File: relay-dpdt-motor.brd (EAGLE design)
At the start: 81.3 x 28.9 mm, 11 parts, among them J1 1X2-3.5MM, J2 1X2-3.5MM, K1 4052, K2 4052

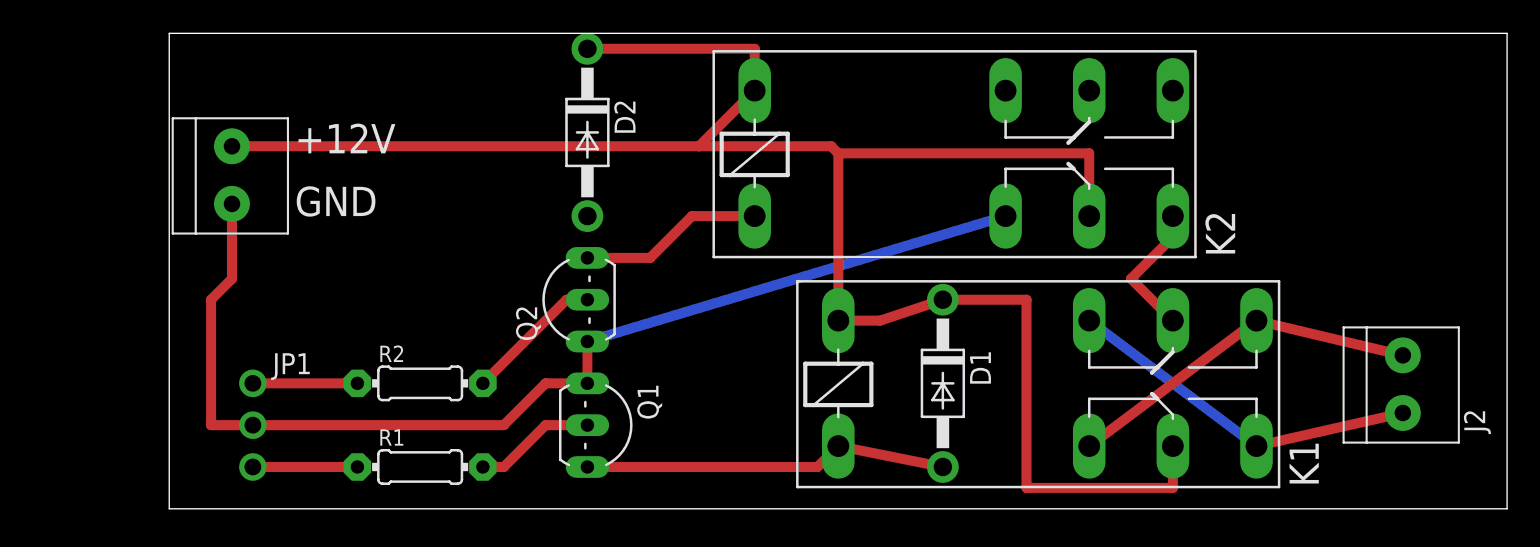
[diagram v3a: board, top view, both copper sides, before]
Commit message: 2 relays one cup, new sim
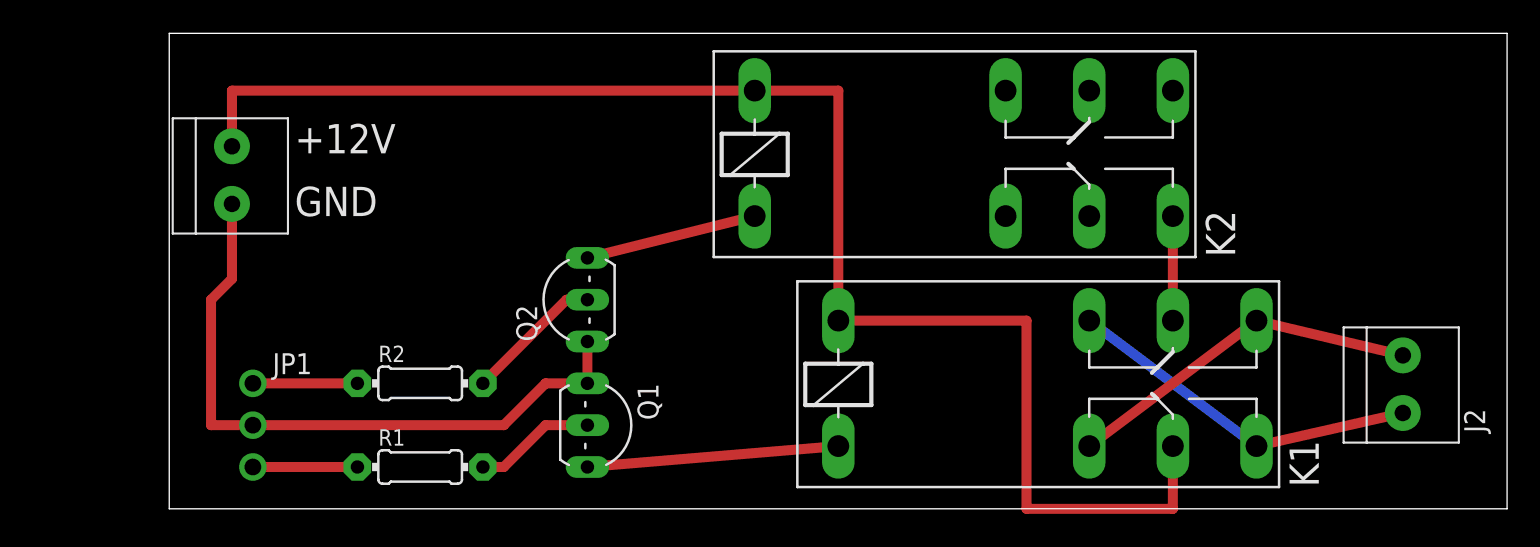
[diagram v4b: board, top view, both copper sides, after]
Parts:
- removed D1, D2: 1N4004, adafruit:DO41-10
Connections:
- removed net N$2: D1.A, K1.2, Q1.3
- new net N$4: K2.2, Q2.3
- net +12V: no longer D1.C, D2.C, K2.P1
- net GND: now also K2.P1; no longer K2.O1
- net N$8: now also K1.2, Q1.3; no longer D2.A, K2.2, Q2.3
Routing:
- net +12V: track 118.2 -> 89.7 mm
- net GND: track 66.9 -> 40.4 mm
- net N$2: track 22.2 -> 0.00 mm
- net N$4: track 0.00 -> 10.5 mm
- net N$8: track 11.2 -> 15.3 mm
- net N$10: track 8.45 -> 6.35 mm
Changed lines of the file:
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@@
 <element name="Q1" library="dp_devices" package="TO-92" value="" x="25.4" y="5.08" rot="R270"/>
 <element name="R1" library="adafruit" package="0204/7" value="" x="15.24" y="2.54"/>
-<element name="D1" library="adafruit" package="DO41-10" value="1N4004" x="46.99" y="7.62" rot="R270"/>
 <element name="J1" library="adafruit" package="1X2-3.5MM" value="1X2-3.5MM" x="3.81" y="20.32" smashed="yes" rot="R270"/>
 <element name="R2" library="adafruit" package="0204/7" value="" x="15.24" y="7.62"/>
@@
 </element>
 <element name="Q2" library="dp_devices" package="TO-92" value="" x="25.4" y="12.7" rot="R90"/>
-<element name="D2" library="adafruit" package="DO41-10" value="1N4004" x="25.4" y="22.86" rot="R270"/>
 </elements>
 <signals>
@@
 <contactref element="K1" pad="P1"/>
 <contactref element="K1" pad="1"/>
-<wire x1="3.81" y1="22.02" x2="32.18" y2="22.02" width="0.6096" layer="1"/>
-<wire x1="32.18" y1="22.02" x2="35.56" y2="25.4" width="0.6096" layer="1"/>
-<wire x1="32.18" y1="22.02" x2="40.21" y2="22.02" width="0.6096" layer="1"/>
-<wire x1="40.21" y1="22.02" x2="40.64" y2="21.59" width="0.6096" layer="1"/>
-<wire x1="40.64" y1="21.59" x2="40.64" y2="11.43" width="0.6096" layer="1"/>
-<wire x1="40.64" y1="11.43" x2="43.18" y2="11.43" width="0.6096" layer="1"/>
-<contactref element="D1" pad="C"/>
-<contactref element="D2" pad="C"/>
-<wire x1="25.4" y1="27.94" x2="35.56" y2="27.94" width="0.6096" layer="1"/>
-<wire x1="35.56" y1="27.94" x2="35.56" y2="25.4" width="0.6096" layer="1"/>
-<wire x1="43.18" y1="11.43" x2="46.99" y2="12.7" width="0.6096" layer="1"/>
-<contactref element="K2" pad="P1"/>
-<wire x1="55.88" y1="17.78" x2="55.88" y2="21.59" width="0.6096" layer="1"/>
-<wire x1="55.88" y1="21.59" x2="40.64" y2="21.59" width="0.6096" layer="1"/>
-<wire x1="60.96" y1="3.81" x2="60.96" y2="1.27" width="0.6096" layer="1"/>
-<wire x1="60.96" y1="1.27" x2="52.07" y2="1.27" width="0.6096" layer="1"/>
-<wire x1="52.07" y1="1.27" x2="52.07" y2="12.7" width="0.6096" layer="1"/>
-<wire x1="52.07" y1="12.7" x2="46.99" y2="12.7" width="0.6096" layer="1"/>
-</signal>
-<signal name="N$2">
-<contactref element="K1" pad="2"/>
-<contactref element="Q1" pad="3"/>
-<wire x1="25.4" y1="2.54" x2="39.37" y2="2.54" width="0.6096" layer="1"/>
-<wire x1="39.37" y1="2.54" x2="40.64" y2="3.81" width="0.6096" layer="1"/>
-<contactref element="D1" pad="A"/>
-<wire x1="40.64" y1="3.81" x2="46.99" y2="2.54" width="0.6096" layer="1"/>
+<wire x1="3.81" y1="22.02" x2="3.81" y2="25.4" width="0.6096" layer="1"/>
+<wire x1="3.81" y1="25.4" x2="35.56" y2="25.4" width="0.6096" layer="1"/>
+<wire x1="35.56" y1="25.4" x2="40.64" y2="25.4" width="0.6096" layer="1"/>
+<wire x1="40.64" y1="25.4" x2="40.64" y2="11.43" width="0.6096" layer="1"/>
+<wire x1="40.64" y1="11.43" x2="52.07" y2="11.43" width="0.6096" layer="1"/>
+<wire x1="60.96" y1="3.81" x2="60.96" y2="0" width="0.6096" layer="1"/>
+<wire x1="60.96" y1="0" x2="52.07" y2="0" width="0.6096" layer="1"/>
+<wire x1="52.07" y1="0" x2="52.07" y2="11.43" width="0.6096" layer="1"/>
 </signal>
 <signal name="GND">
@@
 <contactref element="J1" pad="1"/>
 <contactref element="Q2" pad="1"/>
-<contactref element="K2" pad="O1"/>
 <contactref element="JP1" pad="2"/>
 <wire x1="3.81" y1="18.52" x2="3.81" y2="13.97" width="0.6096" layer="1"/>
@@
 <wire x1="22.86" y1="7.62" x2="25.4" y2="7.62" width="0.6096" layer="1"/>
 <wire x1="25.4" y1="10.16" x2="25.4" y2="7.62" width="0.6096" layer="1"/>
-<wire x1="25.4" y1="10.16" x2="50.8" y2="17.78" width="0.6096" layer="16"/>
+<contactref element="K2" pad="P1"/>
+<wire x1="25.4" y1="10.16" x2="55.88" y2="17.78" width="0" layer="19" extent="1-1"/>
 </signal>
 <signal name="N$3">
@@
 <wire x1="5.08" y1="7.62" x2="11.43" y2="7.62" width="0.6096" layer="1"/>
 </signal>
-<signal name="N$8">
-<contactref element="K2" pad="2"/>
-<contactref element="Q2" pad="3"/>
-<wire x1="25.4" y1="15.24" x2="29.21" y2="15.24" width="0.6096" layer="1"/>
-<wire x1="29.21" y1="15.24" x2="31.75" y2="17.78" width="0.6096" layer="1"/>
-<wire x1="31.75" y1="17.78" x2="35.56" y2="17.78" width="0.6096" layer="1"/>
-<contactref element="D2" pad="A"/>
-<wire x1="25.4" y1="15.24" x2="25.4" y2="17.78" width="0" layer="19" extent="1-1"/>
-</signal>
 <signal name="N$10">
 <contactref element="K1" pad="P2"/>
 <contactref element="K2" pad="S1"/>
-<wire x1="58.42" y1="13.97" x2="60.96" y2="11.43" width="0.6096" layer="1"/>
-<wire x1="60.96" y1="17.78" x2="60.96" y2="16.51" width="0.6096" layer="1"/>
-<wire x1="60.96" y1="16.51" x2="58.42" y2="13.97" width="0.6096" layer="1"/>
+<wire x1="60.96" y1="17.78" x2="60.96" y2="11.43" width="0.6096" layer="1"/>
+</signal>
+<signal name="N$4">
+<contactref element="Q2" pad="3"/>
+<contactref element="K2" pad="2"/>
+<wire x1="25.4" y1="15.24" x2="35.56" y2="17.78" width="0.6096" layer="1"/>
+</signal>
+<signal name="N$8">
+<contactref element="Q1" pad="3"/>
+<contactref element="K1" pad="2"/>
+<wire x1="25.4" y1="2.54" x2="40.64" y2="3.81" width="0.6096" layer="1"/>
 </signal>
 </signals>

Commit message: working relay, but i returned to using the monstermotor shield. and now with beter stop code for the motors
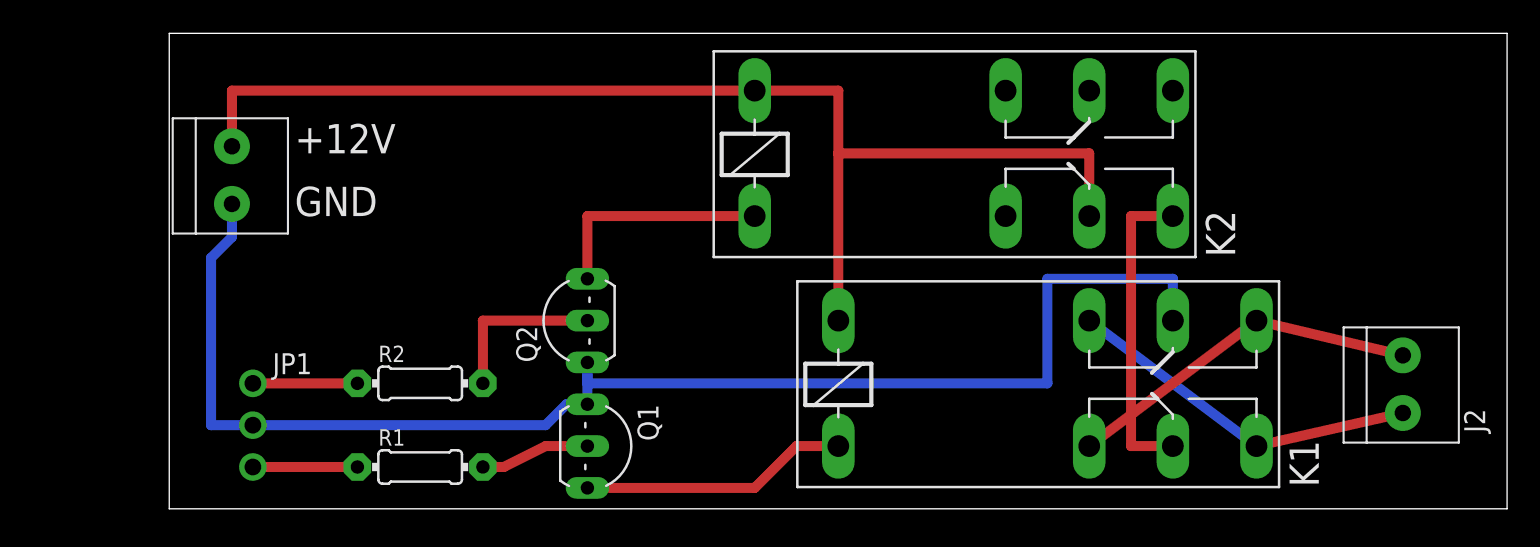
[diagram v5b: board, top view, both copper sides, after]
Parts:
- moved Q1 1.27 mm to (25.4, 3.81)
- moved Q2 1.27 mm to (25.4, 11.4)
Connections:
- removed net N$10: K1.P2, K2.S1
- new net N$2: K1.P1, K2.S1
- net +12V: now also K2.P1; no longer K1.P1
- net GND: now also K1.P2; no longer K2.P1
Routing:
- net GND: track 40.4 -> 85.6 mm
- net N$2: track 0.00 -> 19.0 mm
- net +12V: track 89.7 -> 73.2 mm
- net N$10: track 6.35 -> 0.00 mm
- net N$4: track 10.5 -> 14.0 mm
- net N$3: track 8.45 -> 10.2 mm
- net N$8: track 15.3 -> 16.3 mm
- net N$1: track 7.40 -> 6.65 mm
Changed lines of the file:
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@@
 <attribute name="OC_FARNELL" value="unknown" x="44.45" y="7.62" size="1.778" layer="27" display="off"/>
 </element>
-<element name="Q1" library="dp_devices" package="TO-92" value="" x="25.4" y="5.08" rot="R270"/>
+<element name="Q1" library="dp_devices" package="TO-92" value="" x="25.4" y="3.81" rot="R270"/>
 <element name="R1" library="adafruit" package="0204/7" value="" x="15.24" y="2.54"/>
 <element name="J1" library="adafruit" package="1X2-3.5MM" value="1X2-3.5MM" x="3.81" y="20.32" smashed="yes" rot="R270"/>
@@
 <attribute name="OC_FARNELL" value="unknown" x="39.37" y="21.59" size="1.778" layer="27" display="off"/>
 </element>
-<element name="Q2" library="dp_devices" package="TO-92" value="" x="25.4" y="12.7" rot="R90"/>
+<element name="Q2" library="dp_devices" package="TO-92" value="" x="25.4" y="11.43" rot="R90"/>
 </elements>
 <signals>
@@
 <contactref element="R1" pad="2"/>
 <wire x1="19.05" y1="2.54" x2="20.32" y2="2.54" width="0.6096" layer="1"/>
-<wire x1="20.32" y1="2.54" x2="22.86" y2="5.08" width="0.6096" layer="1"/>
-<wire x1="22.86" y1="5.08" x2="25.4" y2="5.08" width="0.6096" layer="1"/>
+<wire x1="20.32" y1="2.54" x2="22.86" y2="3.81" width="0.6096" layer="1"/>
+<wire x1="22.86" y1="3.81" x2="25.4" y2="3.81" width="0.6096" layer="1"/>
 </signal>
 <signal name="+12V">
 <contactref element="J1" pad="2"/>
 <contactref element="K2" pad="1"/>
-<contactref element="K1" pad="P1"/>
 <contactref element="K1" pad="1"/>
 <wire x1="3.81" y1="22.02" x2="3.81" y2="25.4" width="0.6096" layer="1"/>
 <wire x1="3.81" y1="25.4" x2="35.56" y2="25.4" width="0.6096" layer="1"/>
 <wire x1="35.56" y1="25.4" x2="40.64" y2="25.4" width="0.6096" layer="1"/>
-<wire x1="40.64" y1="25.4" x2="40.64" y2="11.43" width="0.6096" layer="1"/>
-<wire x1="40.64" y1="11.43" x2="52.07" y2="11.43" width="0.6096" layer="1"/>
-<wire x1="60.96" y1="3.81" x2="60.96" y2="0" width="0.6096" layer="1"/>
-<wire x1="60.96" y1="0" x2="52.07" y2="0" width="0.6096" layer="1"/>
-<wire x1="52.07" y1="0" x2="52.07" y2="11.43" width="0.6096" layer="1"/>
+<wire x1="40.64" y1="25.4" x2="40.64" y2="21.59" width="0.6096" layer="1"/>
+<contactref element="K2" pad="P1"/>
+<wire x1="40.64" y1="11.43" x2="40.64" y2="21.59" width="0.6096" layer="1"/>
+<wire x1="40.64" y1="21.59" x2="55.88" y2="21.59" width="0.6096" layer="1"/>
+<wire x1="55.88" y1="21.59" x2="55.88" y2="17.78" width="0.6096" layer="1"/>
 </signal>
 <signal name="GND">
@@
 <contactref element="Q2" pad="1"/>
 <contactref element="JP1" pad="2"/>
-<wire x1="3.81" y1="18.52" x2="3.81" y2="13.97" width="0.6096" layer="1"/>
-<wire x1="3.81" y1="13.97" x2="2.54" y2="12.7" width="0.6096" layer="1"/>
-<wire x1="2.54" y1="12.7" x2="2.54" y2="5.08" width="0.6096" layer="1"/>
-<wire x1="2.54" y1="5.08" x2="5.08" y2="5.08" width="0.6096" layer="1"/>
-<wire x1="5.08" y1="5.08" x2="20.32" y2="5.08" width="0.6096" layer="1"/>
-<wire x1="20.32" y1="5.08" x2="22.86" y2="7.62" width="0.6096" layer="1"/>
-<wire x1="22.86" y1="7.62" x2="25.4" y2="7.62" width="0.6096" layer="1"/>
-<wire x1="25.4" y1="10.16" x2="25.4" y2="7.62" width="0.6096" layer="1"/>
-<contactref element="K2" pad="P1"/>
-<wire x1="25.4" y1="10.16" x2="55.88" y2="17.78" width="0" layer="19" extent="1-1"/>
+<wire x1="3.81" y1="18.52" x2="3.81" y2="16.51" width="0.6096" layer="16"/>
+<wire x1="3.81" y1="16.51" x2="2.54" y2="15.24" width="0.6096" layer="16"/>
+<wire x1="2.54" y1="15.24" x2="2.54" y2="5.08" width="0.6096" layer="16"/>
+<wire x1="2.54" y1="5.08" x2="5.08" y2="5.08" width="0.6096" layer="16"/>
+<wire x1="5.08" y1="5.08" x2="22.86" y2="5.08" width="0.6096" layer="16"/>
+<wire x1="22.86" y1="5.08" x2="24.13" y2="6.35" width="0.6096" layer="16"/>
+<wire x1="24.13" y1="6.35" x2="25.4" y2="6.35" width="0.6096" layer="16"/>
+<wire x1="25.4" y1="6.35" x2="25.4" y2="8.89" width="0.6096" layer="16"/>
+<contactref element="K1" pad="P2"/>
+<wire x1="25.4" y1="8.89" x2="25.4" y2="7.62" width="0.6096" layer="16"/>
+<wire x1="25.4" y1="7.62" x2="53.34" y2="7.62" width="0.6096" layer="16"/>
+<wire x1="53.34" y1="7.62" x2="53.34" y2="13.97" width="0.6096" layer="16"/>
+<wire x1="53.34" y1="13.97" x2="60.96" y2="13.97" width="0.6096" layer="16"/>
+<wire x1="60.96" y1="13.97" x2="60.96" y2="11.43" width="0.6096" layer="16"/>
 </signal>
 <signal name="N$3">
 <contactref element="R2" pad="2"/>
 <contactref element="Q2" pad="2"/>
-<wire x1="19.05" y1="7.62" x2="24.13" y2="12.7" width="0.6096" layer="1"/>
-<wire x1="24.13" y1="12.7" x2="25.4" y2="12.7" width="0.6096" layer="1"/>
+<wire x1="19.05" y1="7.62" x2="19.05" y2="11.43" width="0.6096" layer="1"/>
+<wire x1="19.05" y1="11.43" x2="25.4" y2="11.43" width="0.6096" layer="1"/>
 </signal>
 <signal name="N$6">
@@
 <wire x1="5.08" y1="7.62" x2="11.43" y2="7.62" width="0.6096" layer="1"/>
 </signal>
-<signal name="N$10">
-<contactref element="K1" pad="P2"/>
-<contactref element="K2" pad="S1"/>
-<wire x1="60.96" y1="17.78" x2="60.96" y2="11.43" width="0.6096" layer="1"/>
-</signal>
 <signal name="N$4">
 <contactref element="Q2" pad="3"/>
 <contactref element="K2" pad="2"/>
-<wire x1="25.4" y1="15.24" x2="35.56" y2="17.78" width="0.6096" layer="1"/>
+<wire x1="25.4" y1="13.97" x2="25.4" y2="17.78" width="0.6096" layer="1"/>
+<wire x1="25.4" y1="17.78" x2="35.56" y2="17.78" width="0.6096" layer="1"/>
 </signal>
 <signal name="N$8">
 <contactref element="Q1" pad="3"/>
 <contactref element="K1" pad="2"/>
-<wire x1="25.4" y1="2.54" x2="40.64" y2="3.81" width="0.6096" layer="1"/>
+<wire x1="25.4" y1="1.27" x2="35.56" y2="1.27" width="0.6096" layer="1"/>
+<wire x1="35.56" y1="1.27" x2="38.1" y2="3.81" width="0.6096" layer="1"/>
+<wire x1="38.1" y1="3.81" x2="40.64" y2="3.81" width="0.6096" layer="1"/>
+</signal>
+<signal name="N$2">
+<contactref element="K2" pad="S1"/>
+<contactref element="K1" pad="P1"/>
+<wire x1="60.96" y1="17.78" x2="58.42" y2="17.78" width="0.6096" layer="1"/>
+<wire x1="58.42" y1="17.78" x2="58.42" y2="3.81" width="0.6096" layer="1"/>
+<wire x1="58.42" y1="3.81" x2="60.96" y2="3.81" width="0.6096" layer="1"/>
 </signal>
 </signals>
